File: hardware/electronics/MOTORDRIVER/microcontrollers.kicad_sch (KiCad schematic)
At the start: 31 parts, among them IC8 ATSAME53J18A-MF, U6 ATSAMD11D14A-M, Y1 DSC6001CI2B-025.0000T

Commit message: had to redo some work :<
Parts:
- renumbered C155 to C69, C69 to C70, C70 to C71, C71 to C72, C72 to C73, C73 to C74, C74 to C75, C75 to C76, C76 to C77, C77 to C78, C78 to C79, C79 to C80, C80 to C81, C81 to C82, C82 to C83

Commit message: worked on pcb
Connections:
- no-connect marks 29 -> 30
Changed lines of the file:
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@@
+	)
+	(no_connect
+		(at 140.97 146.05)
 	)
 	(no_connect

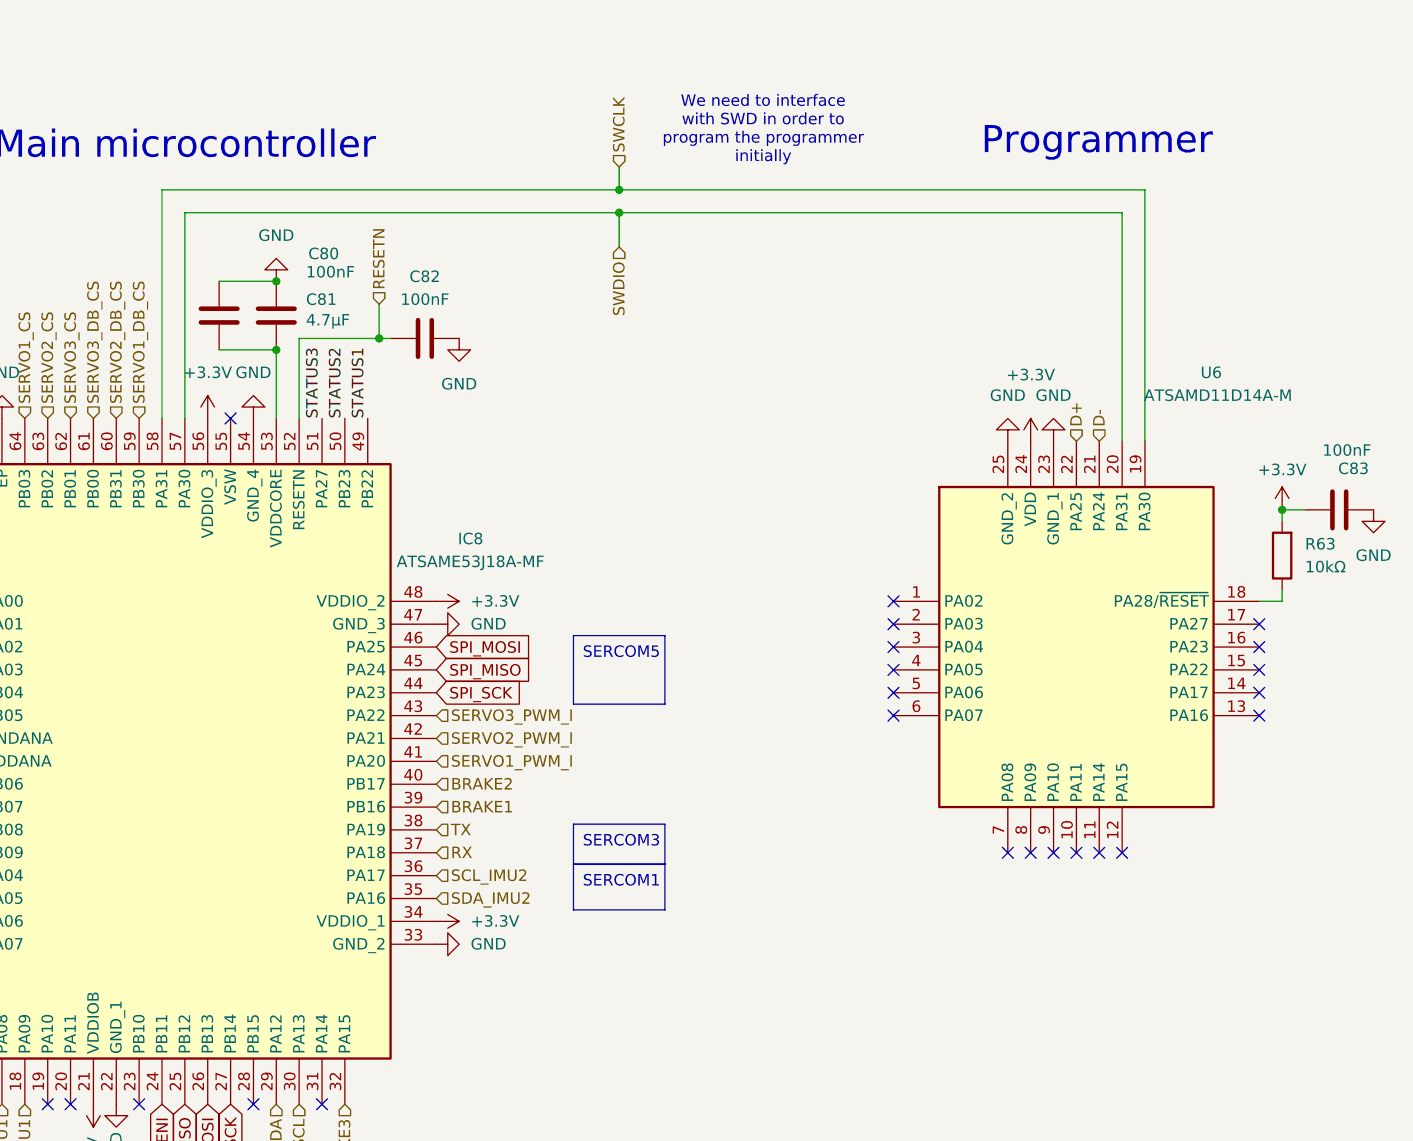
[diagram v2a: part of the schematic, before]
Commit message: worked on pcb and added led to programmer and jumpers to swd line
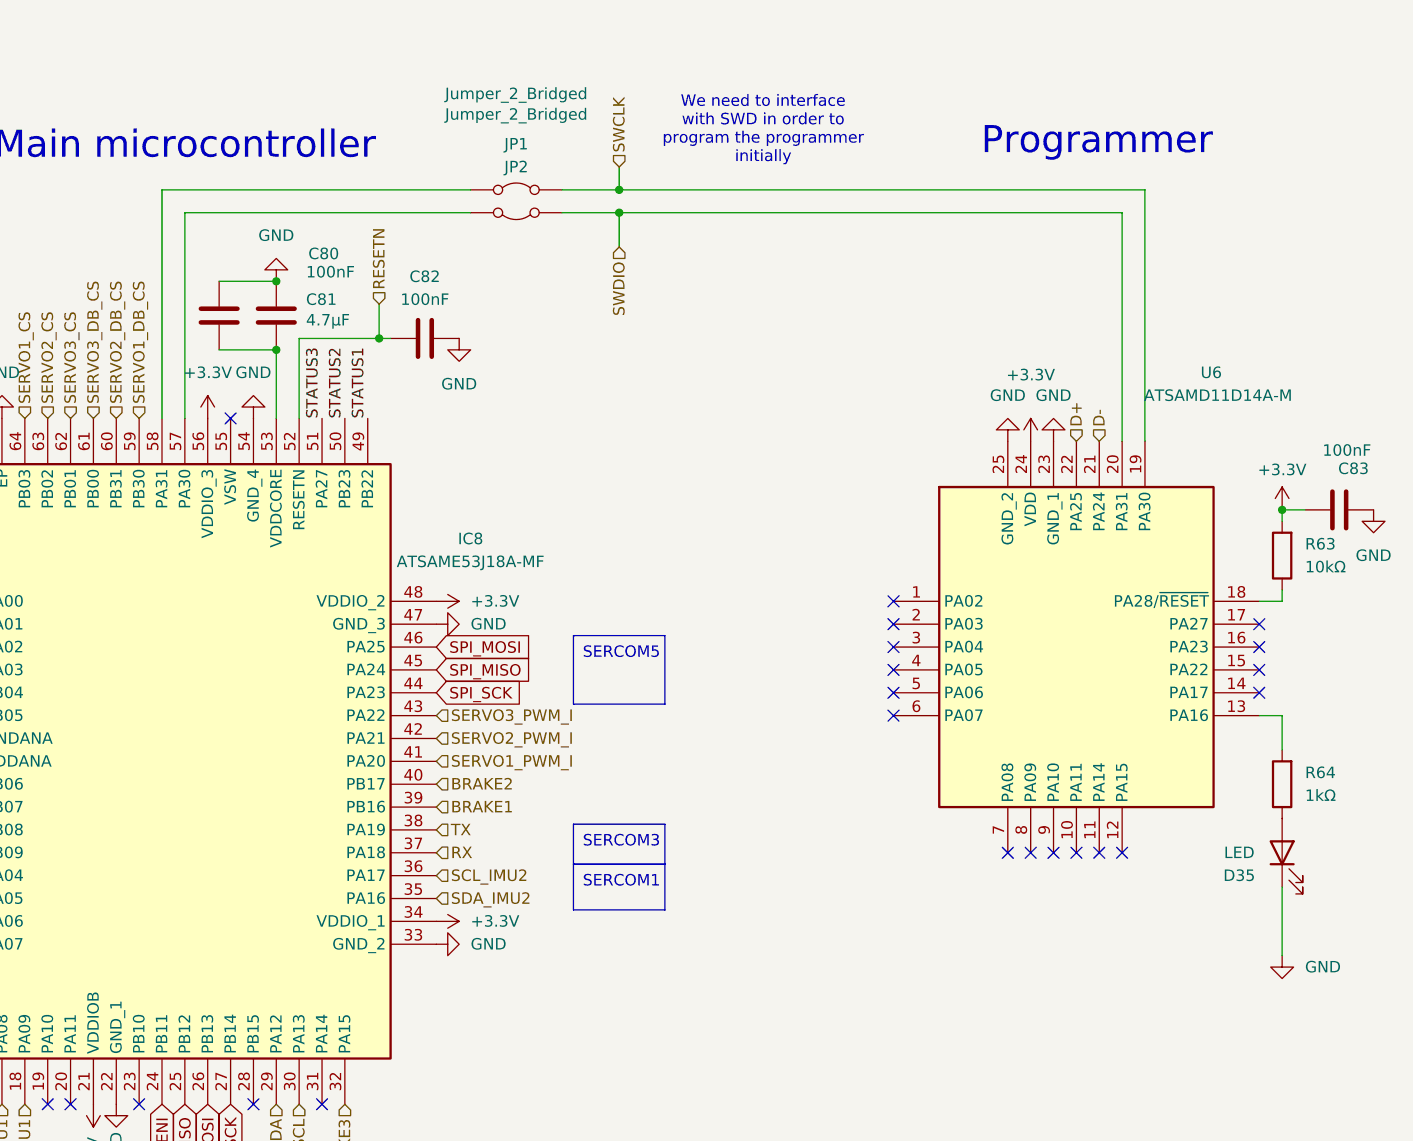
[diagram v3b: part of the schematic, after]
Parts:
- added D35: LED, Diode_SMD:D_0603_1608Metric, symbol Device:LED
- added JP1, JP2: Jumper_2_Bridged, Jumper:SolderJumper-2_P1.3mm_Open_TrianglePad1.0x1.5mm, symbol Jumper:Jumper_2_Bridged
- added R64: 1kΩ, Resistor_SMD:R_0603_1608Metric, symbol Device:R
- Y1: footprint DSC6001CI2B0250000T -> kuben-footprints:DSC6001CI2B0250000T
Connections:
- net GND: now also D35.1 (K)
- net SWCLK: now also JP1.2 (B); no longer IC8.58 (PA31)
- net SWDIO: now also JP2.1 (A); no longer IC8.57 (PA30)
- net at U6.13 (PA16): now also R64.2
- new net: D35.2 (A), R64.1
- new net: IC8.58 (PA31), JP1.1 (A)
- new net: IC8.57 (PA30), JP2.2 (B)
- no-connect marks 30 -> 29
